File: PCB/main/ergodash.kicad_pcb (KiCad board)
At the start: 2 copper layers, 149.9 x 127.4 mm, 94 parts, among them SW1 SW_PUSH, SW10 SW_PUSH, SW11 SW_PUSH, SW12 SW_PUSH, SW13 SW_PUSH, SW14 SW_PUSH, SW15 SW_PUSH, SW16 SW_PUSH, SW17 SW_PUSH, SW18 SW_PUSH, SW19 SW_PUSH, SW2 SW_PUSH, SW20 SW_PUSH, SW21 SW_PUSH, SW22 SW_PUSH, SW23 SW_PUSH, SW24 SW_PUSH, SW25 SW_PUSH, SW26 SW_PUSH, SW27 SW_PUSH, SW28 SW_PUSH, SW3 SW_PUSH, SW30 SW_PUSH, SW31 SW_PUSH, SW32 SW_PUSH, SW33 SW_PUSH, SW34 SW_PUSH, SW35 SW_PUSH, SW36 SW_PUSH, SW38 SW_PUSH, SW39 SW_PUSH, SW4 SW_PUSH, SW40 SW_PUSH, SW41 SW_PUSH, SW5 SW_PUSH, SW6 SW_PUSH, SW7 SW_PUSH, SW8 SW_PUSH, SW9 SW_PUSH

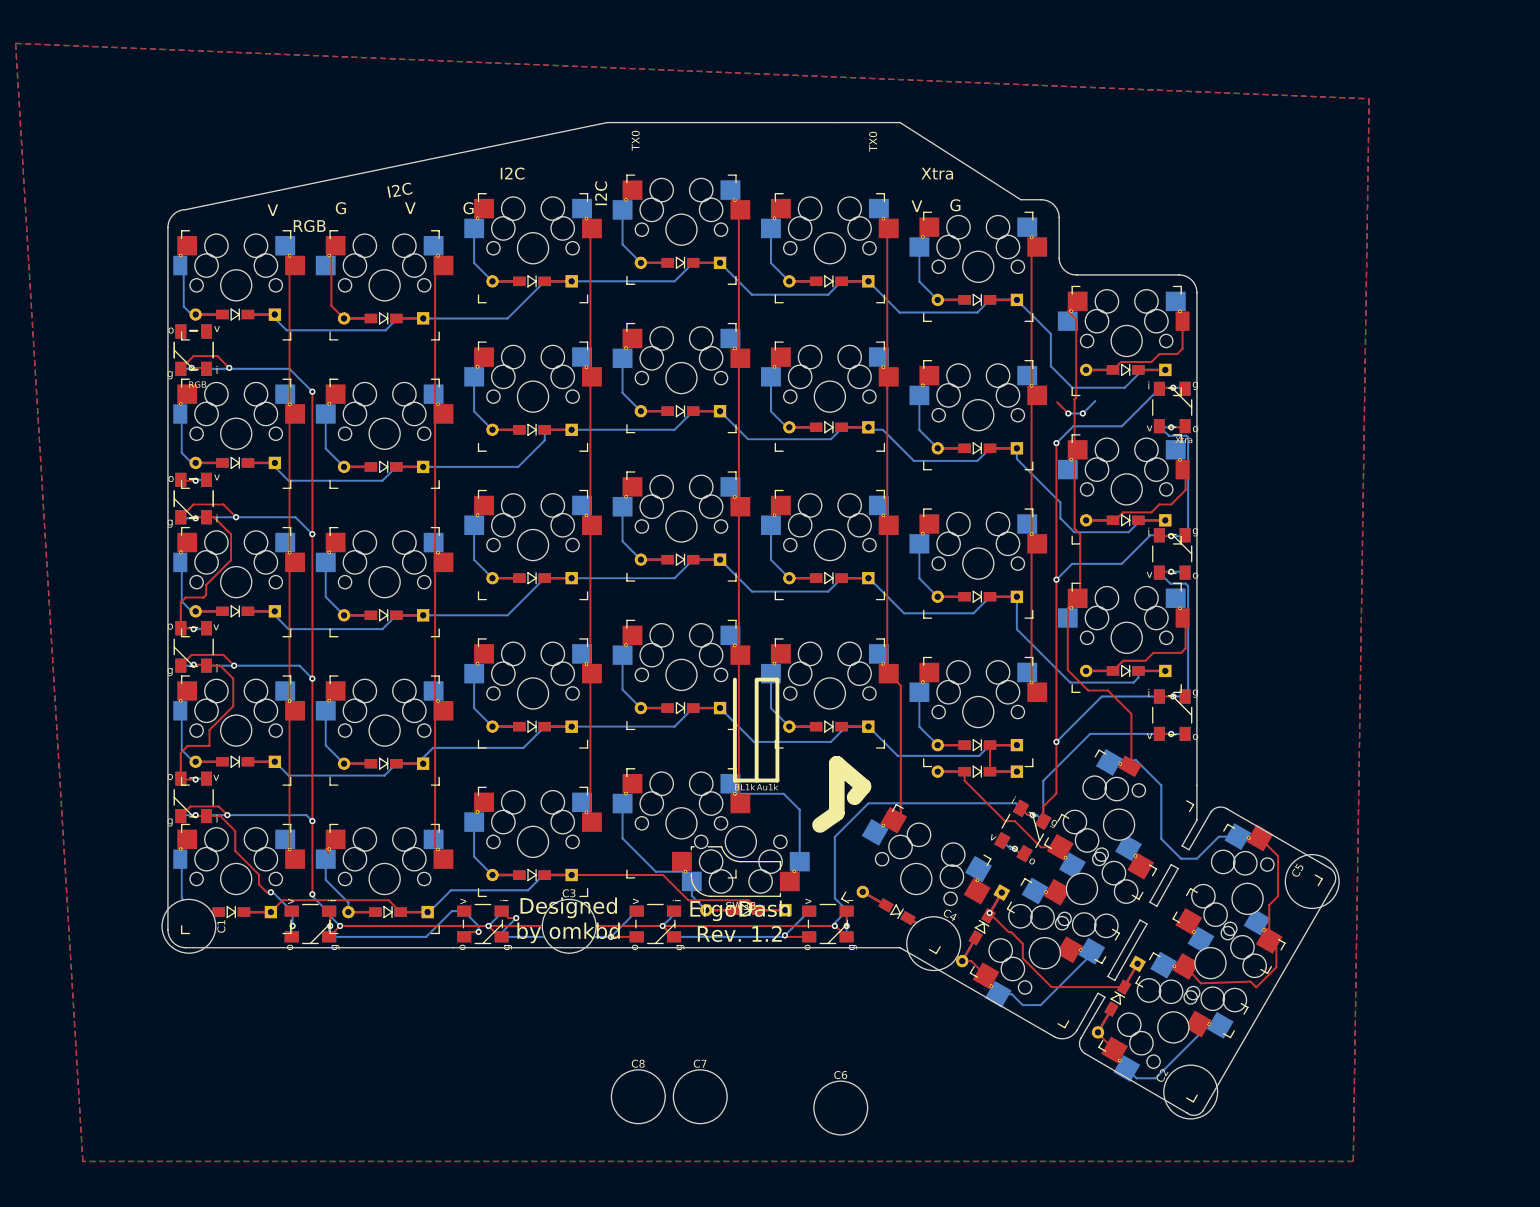
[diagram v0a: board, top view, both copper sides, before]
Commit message: without led
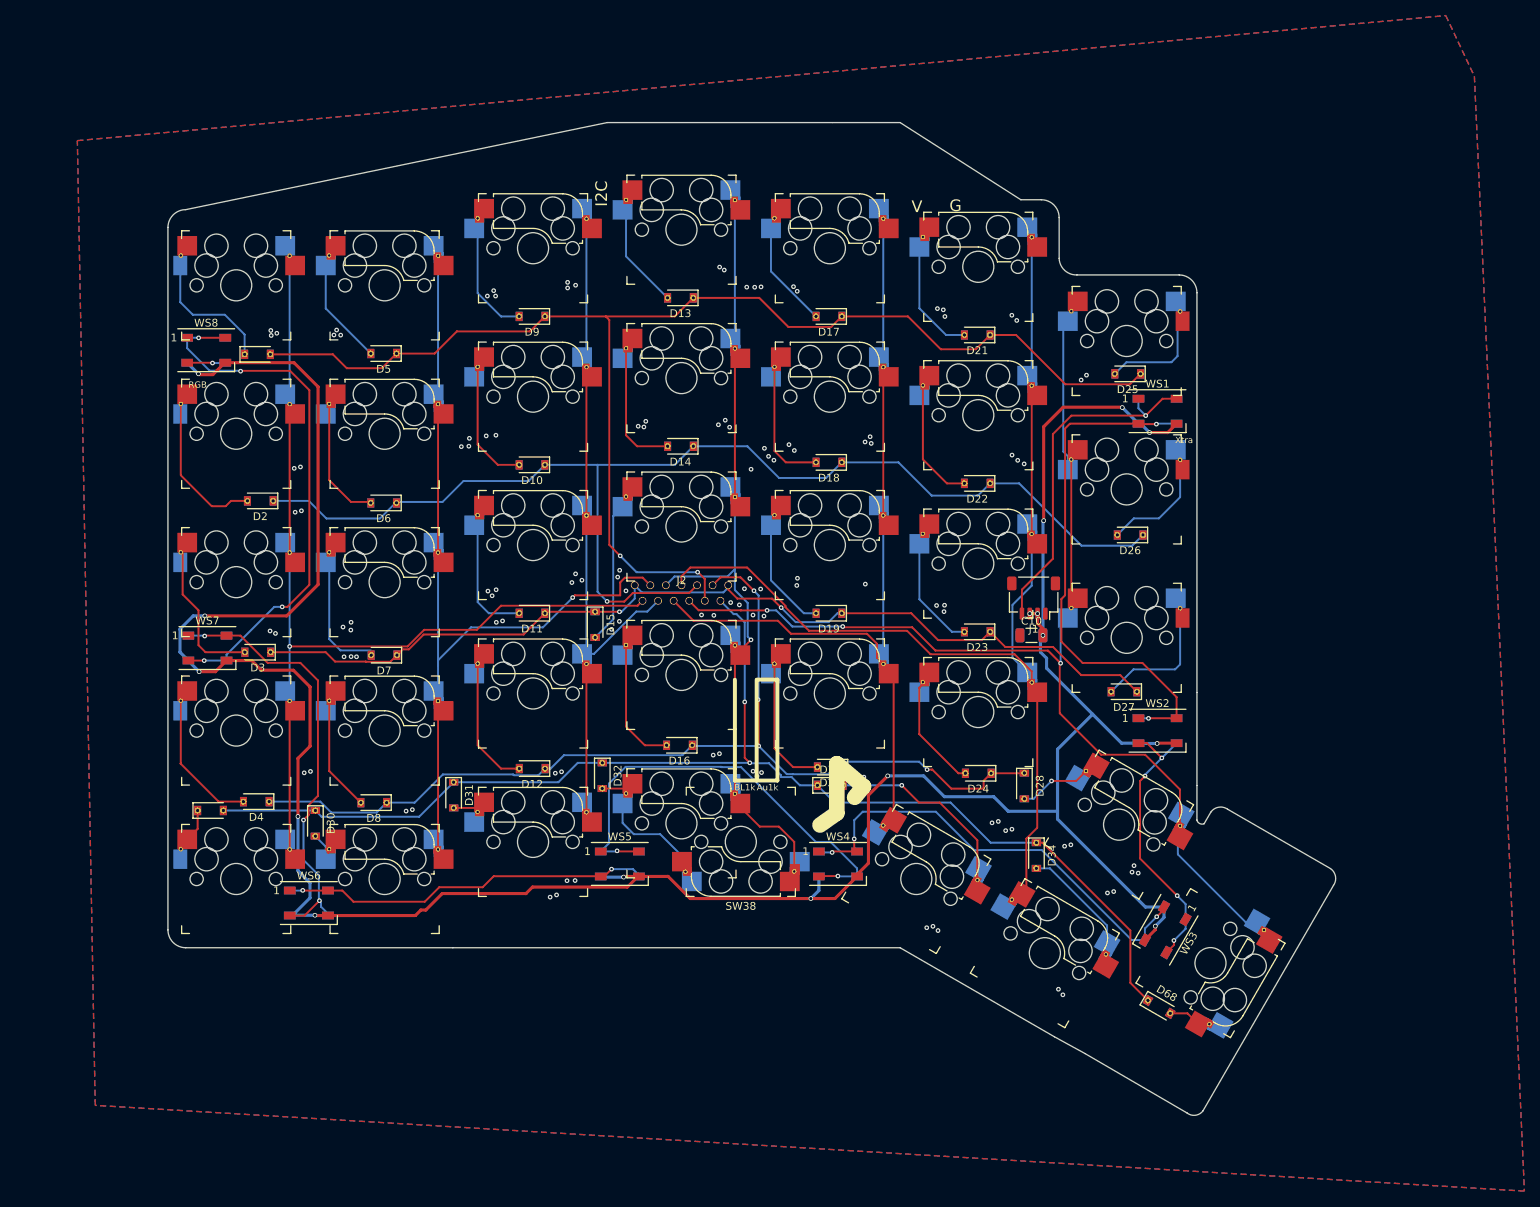
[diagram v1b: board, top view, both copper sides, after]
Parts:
- removed C1, C2, C3, C4, C5, C6, C7, C8: MountingHole, ergodash_2040:Plate_MountingHole_cut
- removed LED1, LED10, LED11, LED12, LED2, LED3, LED4, LED5, LED6, LED7, LED8, LED9: WS2812B, ergodash_2040:WS2812B-5
- removed the SW35 at (190.8, 143.7)
- removed SW39, SW41: SW_PUSH, ergodash_2040:Kailh_socket_MX
- added C10: C, Capacitor_SMD:C_1206_3216Metric, F.Cu at (189.1, 102.9)
- added J1: Conn_01x04, Connector_JST:JST_SH_SM04B-SRSS-TB_1x04-1MP_P1.00mm_Horizontal, F.Cu at (189.3, 98.1)
- added J2: Conn_01x12, ergodash_2040:HDGC_1.0K-J-12PW, F.Cu at (144.1, 98.5)
- added WS1: WS2812B, ergodash_2040:LED_WS2812B_reversible, F.Cu at (205.3, 74.1)
- added WS2: WS2812B, ergodash_2040:LED_WS2812B_reversible, F.Cu at (205.3, 115.1)
- added WS3: WS2812B, ergodash_2040:LED_WS2812B_reversible, F.Cu at (206.2, 140.7)
- added WS4: WS2812B, ergodash_2040:LED_WS2812B_reversible, F.Cu at (164.2, 132.2)
- added WS5: WS2812B, ergodash_2040:LED_WS2812B_reversible, F.Cu at (136.2, 132.2)
- added WS6: WS2812B, ergodash_2040:LED_WS2812B_reversible, F.Cu at (96.3, 137.3)
- added WS7: WS2812B, ergodash_2040:LED_WS2812B_reversible, F.Cu at (83.3, 104.5)
- added WS8: WS2812B, ergodash_2040:LED_WS2812B_reversible, F.Cu at (83.1, 66.3)
- D1, D10, D11, D12, D13, D14, D15, D16, D17, D18, D19, D2, D20, D21, D22, D23, D24, D25, D26, D27, D28, D29, D3, D30, D31, D32, D33, D34, D4, D5, D6, D68, D7, D8, D9: footprint ergodash_2040:Diode_SMD_reversible -> ergodash_2040:D_SOD-123-dobuleside
- SW28: footprint ergodash_2040:Kailh_socket_MX_rightmost -> ergodash_2040:Kailh_socket_MX
- moved D32 25.2 mm to (134.0, 120.9), turned to -90 degrees
- moved D33 18.3 mm to (163.3, 122.2), turned to 0 degrees
- moved D30 14.7 mm to (97.2, 127.0), turned to -90 degrees
- moved D31 14.4 mm to (114.9, 123.4), turned to -90 degrees
- moved D15 13.8 mm to (133.1, 101.5), turned to -90 degrees
- moved D29 13.3 mm to (83.7, 125.4)
- moved D34 11.5 mm to (189.7, 131.2), turned to -90 degrees
- moved SW35 9.53 mm to (190.8, 143.7), turned to -30 degrees
- moved D28 6.32 mm to (188.2, 122.2), turned to -90 degrees
- moved D3 5.99 mm to (89.8, 105.1)
- moved D1 5.86 mm to (89.7, 66.8)
- moved D2 5.84 mm to (90.1, 85.6)
- moved D4 5.79 mm to (89.6, 124.2)
- moved D68 5.42 mm to (205.5, 150.6), turned to -30 degrees
- moved D12 5.39 mm to (125.0, 120.0)
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- renumbered SW36 to SW35
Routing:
- net /col5: track 57.1 -> 137.3 mm
- net /row4: track 83.5 -> 161.2 mm, vias 1 -> 2
- net Net-(WS7-Pad2): track 0.00 -> 69.2 mm, vias 0 -> 4
- net Net-(WS1-Pad2): track 0.00 -> 67.5 mm, vias 0 -> 2
- net /row0: track 110.3 -> 170.4 mm, vias 0 -> 2
- net Net-(WS4-Pad2): track 0.00 -> 58.2 mm, vias 0 -> 2
- net Net-(WS4-Pad4): track 0.00 -> 58.0 mm, vias 0 -> 3
- net Net-(WS6-Pad2): track 0.00 -> 55.8 mm, vias 0 -> 3
- net Net-(WS5-Pad2): track 0.00 -> 47.0 mm, vias 0 -> 2
- net /row1: track 109.9 -> 155.7 mm, vias 0 -> 1
- net /RGB: track 0.00 -> 45.0 mm, vias 0 -> 1
- net /col0: track 76.2 -> 120.2 mm, vias 0 -> 1
- net /row3: track 91.3 -> 132.8 mm, vias 0 -> 4
- net Net-(WS2-Pad2): track 0.00 -> 36.0 mm, vias 0 -> 4
- net /col1: track 76.0 -> 108.8 mm, vias 0 -> 1
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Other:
- outline, holes or cut-outs redrawn
- rule pad_to_mask_clearance: 0.2 -> 0
- board text removed: "Designed by omkbd"
- board text removed: "ErgoDash Rev. 1.2"
- board text removed: "TX0"
